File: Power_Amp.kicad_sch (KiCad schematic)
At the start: 22 parts, among them J10 2118718-2, J11 Molex 73251-1153, P13 CONUFL001-SMD-T, U27 TQP7M9106

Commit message: More notes and minor changes
Signed-off-by: Corey Minyard <corey@minyard.net>
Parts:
- removed R80: 0, Resistor_SMD:R_0603_1608Metric_Pad0.98x0.95mm_HandSolder, symbol Device:R
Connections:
- net at FL2.8 (INPUT): now also C117.2, L38.1
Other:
- note added: "2W (33dBm) into 50 ohms is 10V RMS, ~14.3V peak to peak on the right side of the impedance converter. Pick appropriate devices."
- moved on the sheet: FL2, J11, L39

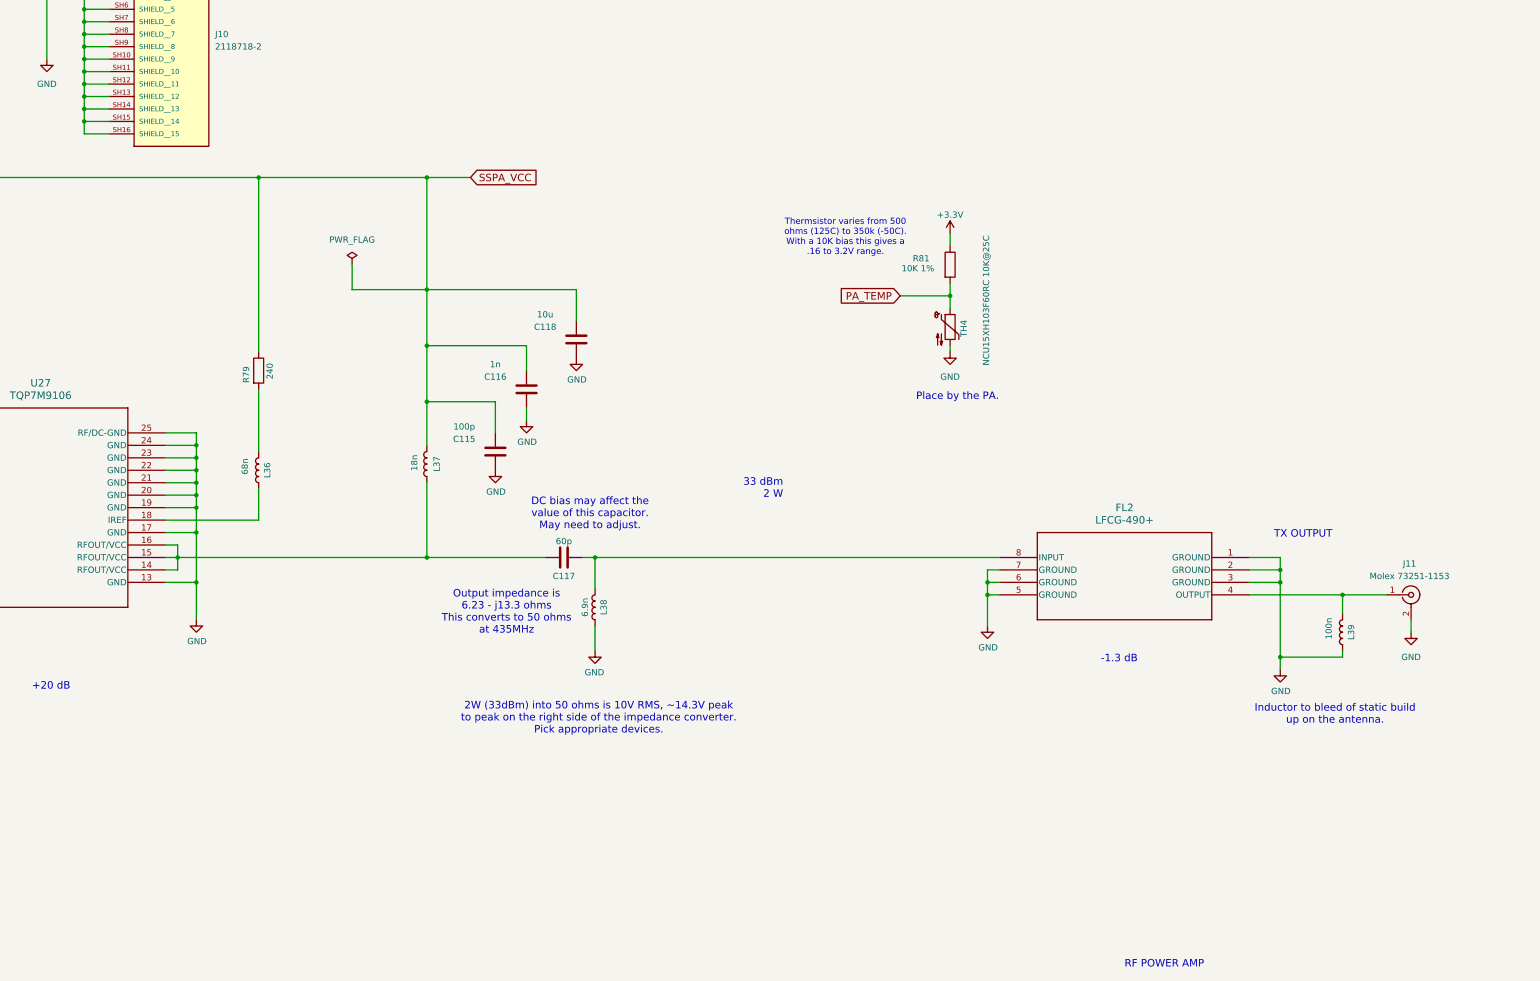
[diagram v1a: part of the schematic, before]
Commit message: Add power measurement on TX
Add chips for forward and reverse power.

Signed-off-by: Corey Minyard <corey@minyard.net>
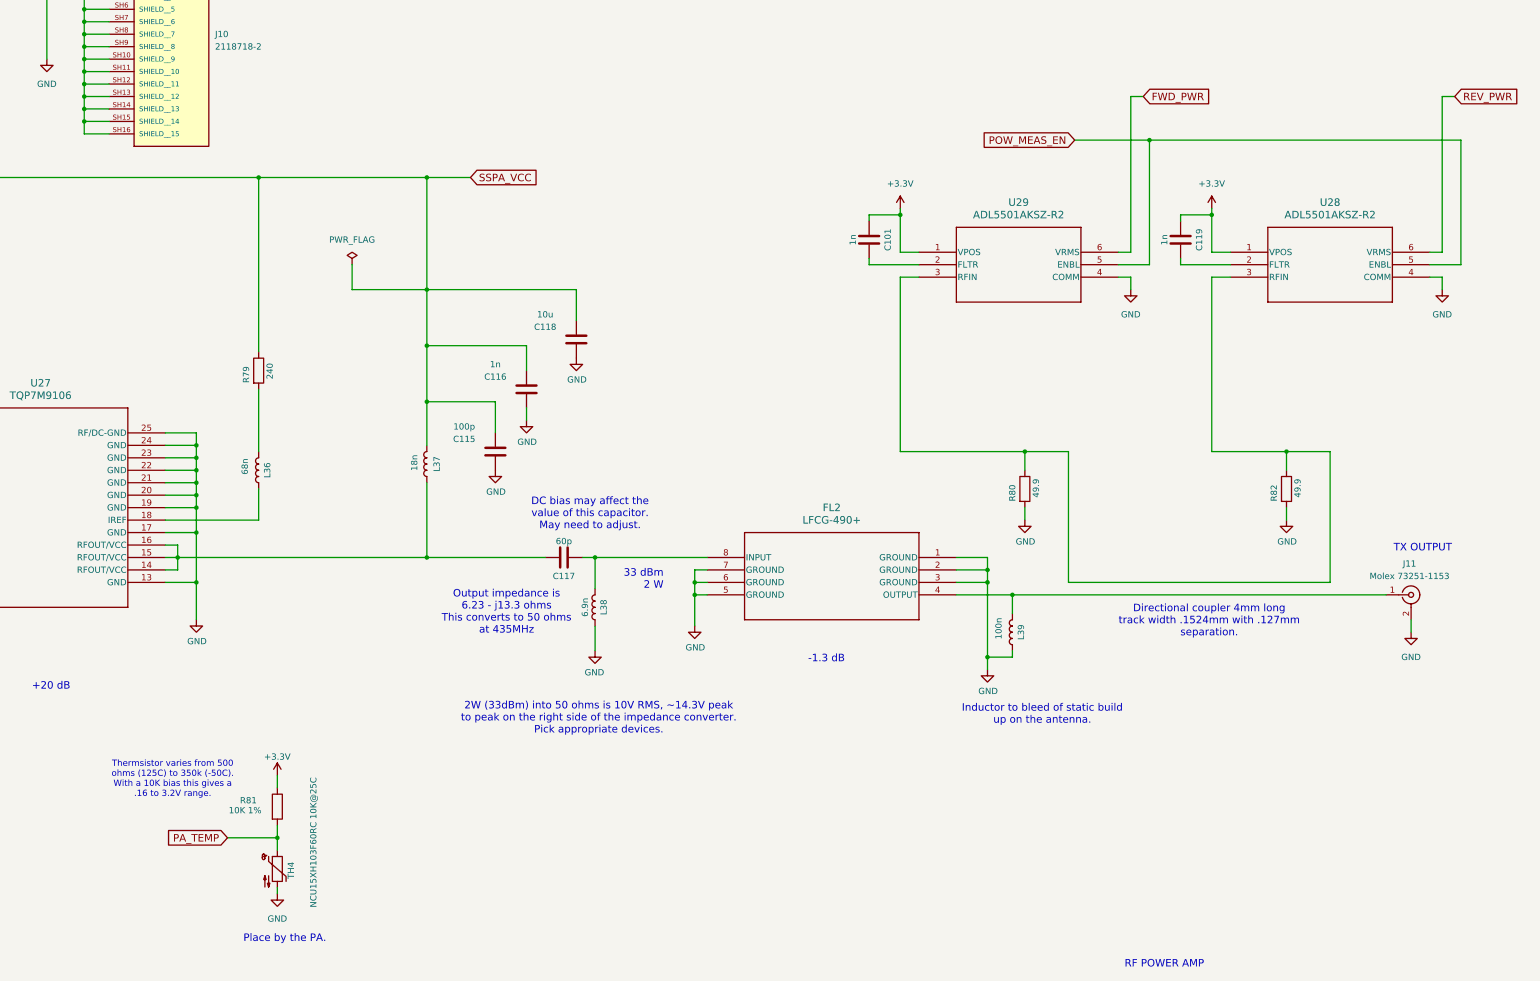
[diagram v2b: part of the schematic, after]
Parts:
- added C101, C119: 1n, Capacitor_SMD:C_0603_1608Metric_Pad1.08x0.95mm_HandSolder, symbol Device:C
- added R80, R82: 49.9, Resistor_SMD:R_0603_1608Metric_Pad0.98x0.95mm_HandSolder, symbol Device:R
- added U28, U29: ADL5501AKSZ-R2, PacSatDev_misc:KS-6_ADI, symbol PACSAT_ICs:ADL5501AKSZ-R2
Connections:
- net +3.3V: now also C101.2, C119.2, U28.1 (VPOS), U29.1 (VPOS)
- net GND: now also R80.2, R82.2, U28.4 (COMM), U29.4 (COMM)
- new net: C101.1, U29.2 (FLTR)
- new net: R80.1, R82.1, U28.3 (RFIN), U29.3 (RFIN)
- new net: C119.1, U28.2 (FLTR)
- new net FWD_PWR: U29.6 (VRMS)
- new net POW_MEAS_EN: U28.5 (ENBL), U29.5 (ENBL)
- new net REV_PWR: U28.6 (VRMS)
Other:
- note added: "Directional coupler 4mm long track width .1524mm with .127mm separation."
- moved on the sheet: FL2, L39, R81, TH4

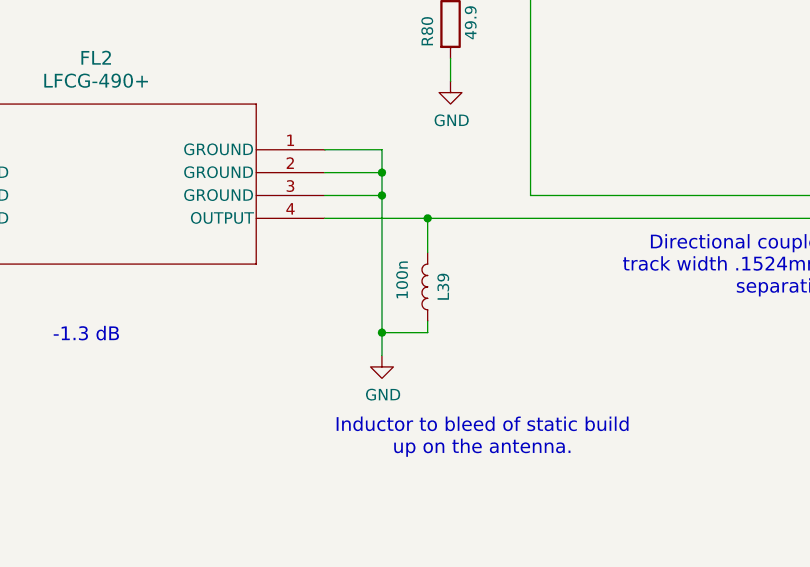
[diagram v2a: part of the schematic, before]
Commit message: Change TX bleed off inductor to bigger one
100nH really isn't big enough.

Signed-off-by: Corey Minyard <corey@minyard.net>
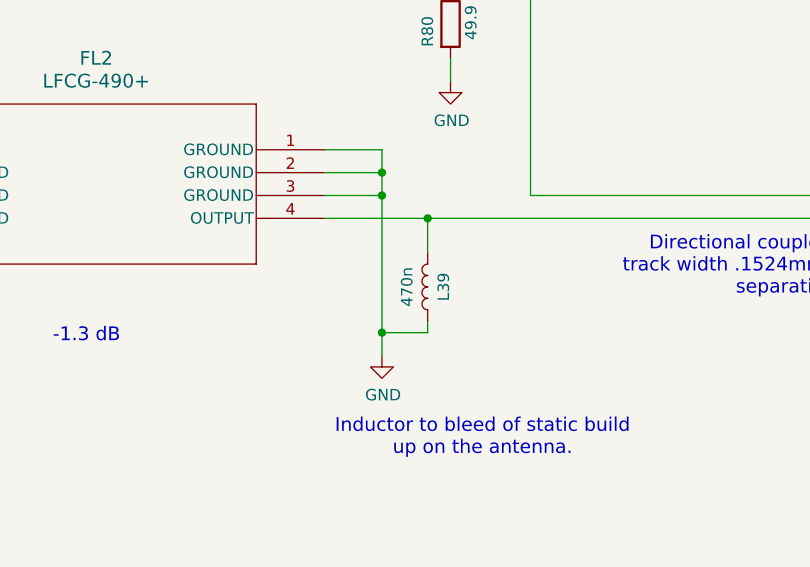
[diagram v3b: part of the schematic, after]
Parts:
- L39: value 100n -> 470n; footprint Inductor_SMD:L_0603_1608Metric_Pad1.05x0.95mm_HandSolder -> Inductor_SMD:L_0805_2012Metric_Pad1.15x1.40mm_HandSolder
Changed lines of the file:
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@@
 			)
 		)
-		(property "Value" "100n"
-			(at 310.896 174.498 90)
+		(property "Value" "470n"
+			(at 311.404 175.26 90)
 			(effects
 				(font
@@
 			)
 		)
-		(property "Footprint" "Inductor_SMD:L_0603_1608Metric_Pad1.05x0.95mm_HandSolder"
+		(property "Footprint" "Inductor_SMD:L_0805_2012Metric_Pad1.15x1.40mm_HandSolder"
 			(at 313.69 175.26 0)
 			(effects

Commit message: Check over notes and some component values
Fix a wrong capacitor in one spot, set Q and voltage as necessary.

Signed-off-by: Corey Minyard <corey@minyard.net>
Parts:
- added C57: 4p 1% 30V, Capacitor_SMD:C_0603_1608Metric_Pad1.08x0.95mm_HandSolder, symbol Device:C
- C114: value 37p -> 37p 1%
- C117: value 60p -> 110p 1% 30V
- L35: value 17n -> 17n 2% Q>=40
- L38: value 6.9n -> 6.8n 2% Q=40
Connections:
- net at C117.2, FL2.8 (INPUT), L38.1: now also C57.2
- net at C117.1, L37.1, U27.14 (RFOUT/VCC)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: now also C57.1
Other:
- note removed: "Class AB Use Hi Q Caps in all matching circuits (Ultra low ESR at 435 MHz)"
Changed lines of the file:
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@@
 	(text "DC bias may affect the\nvalue of this capacitor.\nMay need to adjust."
 		(exclude_from_sim no)
-		(at 227.584 151.13 0)
+		(at 243.078 155.194 0)
 		(effects
 			(font
@@
 		)
 	)
-	(text "\nClass AB \n\n\nUse Hi Q Caps in all matching circuits (Ultra low ESR at 435 MHz)"
-		(exclude_from_sim no)
-		(at 32.385 238.125 0)
-		(effects
-			(font
-				(size 1.524 1.524)
-			)
-			(justify left bottom)
-		)
-	)
 	(text "Output impedance is\n6.23 - j13.3 ohms\nThis converts to 50 ohms\nat 435MHz"
 		(exclude_from_sim no)
@@
 		(color 0 0 0 0)
 	)
+	(junction
+		(at 214.63 160.02)
+		(diameter 0)
+		(color 0 0 0 0)
+	)
 	(wire
 		(pts
@@
 	(wire
 		(pts
+			(xy 228.6 149.86) (xy 228.6 160.02)
+		)
+		(stroke
+			(width 0)
+			(type default)
+		)
+	)
+	(wire
+		(pts
 			(xy 143.51 160.02) (xy 194.31 160.02)
 		)
@@
 	(wire
 		(pts
+			(xy 214.63 149.86) (xy 214.63 160.02)
+		)
+		(stroke
+			(width 0)
+			(type default)
+		)
+	)
+	(wire
+		(pts
 			(xy 313.69 167.64) (xy 302.26 167.64)
 		)
@@
 	(wire
 		(pts
-			(xy 218.44 160.02) (xy 194.31 160.02)
+			(xy 218.44 160.02) (xy 214.63 160.02)
 		)
 		(stroke
@@
 	(wire
 		(pts
+			(xy 218.44 149.86) (xy 214.63 149.86)
+		)
+		(stroke
+			(width 0)
+			(type default)
+		)
+	)
+	(wire
+		(pts
 			(xy 194.31 82.55) (xy 194.31 105.41)
 		)
@@
 	(wire
 		(pts
+			(xy 214.63 160.02) (xy 194.31 160.02)
+		)
+		(stroke
+			(width 0)
+			(type default)
+		)
+	)
+	(wire
+		(pts
 			(xy 124.46 45.72) (xy 124.46 43.18)
 		)
@@
 	(wire
 		(pts
+			(xy 226.06 149.86) (xy 228.6 149.86)
+		)
+		(stroke
+			(width 0)
+			(type default)
+		)
+	)
+	(wire
+		(pts
 			(xy 398.78 102.87) (xy 401.32 102.87)
 		)
@@
 			)
 		)
-		(property "Value" "37p"
+		(property "Value" "37p 1%"
 			(at 78.74 154.94 0)
 			(effects
@@
 	)
 	(symbol
+		(lib_id "Device:C")
+		(at 222.25 149.86 90)
+		(mirror x)
+		(unit 1)
+		(exclude_from_sim no)
+		(in_bom yes)
+		(on_board yes)
+		(dnp no)
+		(property "Reference" "C57"
+			(at 222.25 153.67 90)
+			(effects
+				(font
+					(size 1.27 1.27)
+				)
+			)
+		)
+		(property "Value" "4p 1% 30V"
+			(at 222.25 146.558 90)
+			(effects
+				(font
+					(size 1.27 1.27)
+				)
+			)
+		)
+		(property "Footprint" "Capacitor_SMD:C_0603_1608Metric_Pad1.08x0.95mm_HandSolder"
+			(at 226.06 150.8252 0)
+			(effects
+				(font
+					(size 1.27 1.27)
+				)
+				(hide yes)
+			)
+		)
+		(property "Datasheet" "~"
+			(at 222.25 149.86 0)
+			(effects
+				(font
+					(size 1.27 1.27)
+				)
+				(hide yes)
+			)
+		)
+		(property "Description" ""
+			(at 222.25 149.86 0)
+			(effects
+				(font
+					(size 1.27 1.27)
+				)
+			)
+		)
+		(pin "1"
+		)
+		(pin "2"
+		)
+		(instances
+			(project "PacSat_AFSK"
+				(path "/cc9f42d2-6985-41ac-acab-5ab7b01c5b38/b85b88c3-87c5-49e2-804e-0759552ace3d"
+					(reference "C57")
+					(unit 1)
+				)
+			)
+		)
+	)
+	(symbol
 		(lib_id "power:GND")
 		(at 116.84 58.42 0)
@@
 			)
 		)
-		(property "Value" "60p"
+		(property "Value" "110p 1% 30V"
 			(at 222.25 156.718 90)
 			(effects
@@
 			)
 		)
-		(property "Value" "6.9n"
+		(property "Value" "6.8n 2% Q=40"
 			(at 226.568 170.18 90)
 			(effects
@@
 			)
 		)
-		(property "Value" "17n"
-			(at 79.502 139.446 90)
+		(property "Value" "17n 2% Q>=40"
+			(at 75.184 140.208 90)
 			(effects
 				(font

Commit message: Adjust the TX output impedance match some more
Signed-off-by: Corey Minyard <corey@minyard.net>
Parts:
- removed C57: 4p 1% 30V, Capacitor_SMD:C_0603_1608Metric_Pad1.08x0.95mm_HandSolder, symbol Device:C
- C117: value 110p 1% 30V -> 130p 1% 30V
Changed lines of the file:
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@@
 		(color 0 0 0 0)
 	)
-	(junction
-		(at 214.63 160.02)
-		(diameter 0)
-		(color 0 0 0 0)
-	)
 	(wire
 		(pts
@@
 	(wire
 		(pts
-			(xy 228.6 149.86) (xy 228.6 160.02)
-		)
-		(stroke
-			(width 0)
-			(type default)
-		)
-	)
-	(wire
-		(pts
 			(xy 143.51 160.02) (xy 194.31 160.02)
 		)
@@
 	(wire
 		(pts
-			(xy 214.63 149.86) (xy 214.63 160.02)
-		)
-		(stroke
-			(width 0)
-			(type default)
-		)
-	)
-	(wire
-		(pts
 			(xy 313.69 167.64) (xy 302.26 167.64)
 		)
@@
 	(wire
 		(pts
-			(xy 218.44 160.02) (xy 214.63 160.02)
+			(xy 194.31 160.02) (xy 218.44 160.02)
 		)
 		(stroke
@@
 	(wire
 		(pts
-			(xy 218.44 149.86) (xy 214.63 149.86)
-		)
-		(stroke
-			(width 0)
-			(type default)
-		)
-	)
-	(wire
-		(pts
 			(xy 194.31 82.55) (xy 194.31 105.41)
 		)
@@
 	(wire
 		(pts
-			(xy 214.63 160.02) (xy 194.31 160.02)
-		)
-		(stroke
-			(width 0)
-			(type default)
-		)
-	)
-	(wire
-		(pts
 			(xy 124.46 45.72) (xy 124.46 43.18)
 		)
@@
 	(wire
 		(pts
-			(xy 226.06 149.86) (xy 228.6 149.86)
-		)
-		(stroke
-			(width 0)
-			(type default)
-		)
-	)
-	(wire
-		(pts
 			(xy 398.78 102.87) (xy 401.32 102.87)
 		)
@@
 	)
 	(symbol
-		(lib_id "Device:C")
-		(at 222.25 149.86 90)
-		(mirror x)
-		(unit 1)
-		(exclude_from_sim no)
-		(in_bom yes)
-		(on_board yes)
-		(dnp no)
-		(property "Reference" "C57"
-			(at 222.25 153.67 90)
-			(effects
-				(font
-					(size 1.27 1.27)
-				)
-			)
-		)
-		(property "Value" "4p 1% 30V"
-			(at 222.25 146.558 90)
-			(effects
-				(font
-					(size 1.27 1.27)
-				)
-			)
-		)
-		(property "Footprint" "Capacitor_SMD:C_0603_1608Metric_Pad1.08x0.95mm_HandSolder"
-			(at 226.06 150.8252 0)
-			(effects
-				(font
-					(size 1.27 1.27)
-				)
-				(hide yes)
-			)
-		)
-		(property "Datasheet" "~"
-			(at 222.25 149.86 0)
-			(effects
-				(font
-					(size 1.27 1.27)
-				)
-				(hide yes)
-			)
-		)
-		(property "Description" ""
-			(at 222.25 149.86 0)
-			(effects
-				(font
-					(size 1.27 1.27)
-				)
-			)
-		)
-		(pin "1"
-		)
-		(pin "2"
-		)
-		(instances
-			(project "PacSat_AFSK"
-				(path "/cc9f42d2-6985-41ac-acab-5ab7b01c5b38/b85b88c3-87c5-49e2-804e-0759552ace3d"
-					(reference "C57")
-					(unit 1)
-				)
-			)
-		)
-	)
-	(symbol
 		(lib_id "power:GND")
 		(at 116.84 58.42 0)
@@
 			)
 		)
-		(property "Value" "110p 1% 30V"
+		(property "Value" "130p 1% 30V"
 			(at 222.25 156.718 90)
 			(effects

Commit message: More work on the LNA/PA impedance matchers
Did some simulations, found some issues.

Signed-off-by: Corey Minyard <corey@minyard.net>
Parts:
- C114: value 37p 1% -> 39p 1%
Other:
- moved on the sheet: C114, L35
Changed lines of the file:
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@@
 	(text "Input impedance is\n1.87 - 37.7j this\nmatches to 50 ohms\nat 435MHz."
 		(exclude_from_sim no)
-		(at 57.404 154.94 0)
+		(at 66.04 172.72 0)
 		(effects
 			(font
@@
 	)
 	(junction
-		(at 72.39 142.24)
-		(diameter 0)
-		(color 0 0 0 0)
-	)
-	(junction
 		(at 194.31 116.84)
 		(diameter 0)
@@
 	)
 	(junction
+		(at 58.42 142.24)
+		(diameter 0)
+		(color 0 0 0 0)
+	)
+	(junction
 		(at 83.82 162.56)
 		(diameter 0)
@@
 	(wire
 		(pts
-			(xy 50.8 142.24) (xy 72.39 142.24)
+			(xy 50.8 142.24) (xy 58.42 142.24)
 		)
 		(stroke
@@
 	(wire
 		(pts
-			(xy 72.39 142.24) (xy 74.93 142.24)
-		)
-		(stroke
-			(width 0)
-			(type default)
-		)
-	)
-	(wire
-		(pts
 			(xy 82.55 115.57) (xy 68.58 115.57)
 		)
@@
 	(wire
 		(pts
+			(xy 58.42 142.24) (xy 58.42 148.59)
+		)
+		(stroke
+			(width 0)
+			(type default)
+		)
+	)
+	(wire
+		(pts
 			(xy 369.57 138.43) (xy 369.57 142.24)
 		)
@@
 	(wire
 		(pts
+			(xy 69.85 142.24) (xy 87.63 142.24)
+		)
+		(stroke
+			(width 0)
+			(type default)
+		)
+	)
+	(wire
+		(pts
 			(xy 87.63 144.78) (xy 87.63 142.24)
 		)
@@
 	(wire
 		(pts
+			(xy 58.42 156.21) (xy 58.42 161.29)
+		)
+		(stroke
+			(width 0)
+			(type default)
+		)
+	)
+	(wire
+		(pts
 			(xy 124.46 55.88) (xy 124.46 53.34)
 		)
@@
 	(wire
 		(pts
-			(xy 72.39 156.21) (xy 72.39 161.29)
-		)
-		(stroke
-			(width 0)
-			(type default)
-		)
-	)
-	(wire
-		(pts
 			(xy 82.55 82.55) (xy 160.02 82.55)
 		)
@@
 	(wire
 		(pts
-			(xy 82.55 142.24) (xy 87.63 142.24)
+			(xy 58.42 142.24) (xy 62.23 142.24)
 		)
 		(stroke
@@
 	(wire
 		(pts
-			(xy 72.39 142.24) (xy 72.39 148.59)
-		)
-		(stroke
-			(width 0)
-			(type default)
-		)
-	)
-	(wire
-		(pts
 			(xy 354.33 102.87) (xy 358.14 102.87)
 		)
@@
 	(symbol
 		(lib_id "Device:C")
-		(at 72.39 152.4 0)
+		(at 58.42 152.4 0)
 		(unit 1)
 		(exclude_from_sim no)
@@
 		(dnp no)
 		(property "Reference" "C114"
-			(at 77.47 152.4 0)
+			(at 63.5 152.4 0)
 			(effects
 				(font
@@
 			)
 		)
-		(property "Value" "37p 1%"
-			(at 78.74 154.94 0)
+		(property "Value" "39p 1%"
+			(at 64.77 154.94 0)
 			(effects
 				(font
@@
 		)
 		(property "Footprint" "Capacitor_SMD:C_0603_1608Metric_Pad1.08x0.95mm_HandSolder"
-			(at 73.3552 156.21 0)
+			(at 59.3852 156.21 0)
 			(effects
 				(font
@@
 		)
 		(property "Datasheet" "~"
-			(at 72.39 152.4 0)
+			(at 58.42 152.4 0)
 			(effects
 				(font
@@
 		)
 		(property "Description" ""
-			(at 72.39 152.4 0)
+			(at 58.42 152.4 0)
 			(effects
 				(font
@@
 		)
 		(instances
-			(project "PacSat_Dev_RevD_240614"
+			(project "PacSat_AFSK"
 				(path "/cc9f42d2-6985-41ac-acab-5ab7b01c5b38/b85b88c3-87c5-49e2-804e-0759552ace3d"
 					(reference "C114")
@@
 	(symbol
 		(lib_id "power:GND")
-		(at 72.39 161.29 0)
+		(at 58.42 161.29 0)
 		(unit 1)
 		(exclude_from_sim no)
@@
 		(dnp no)
 		(property "Reference" "#PWR0222"
-			(at 72.39 167.64 0)
+			(at 58.42 167.64 0)
 			(effects
 				(font
@@
 		)
 		(property "Value" "GND"
-			(at 72.517 165.6842 0)
+			(at 58.547 165.6842 0)
 			(effects
 				(font
@@
 		)
 		(property "Footprint" ""
-			(at 72.39 161.29 0)
+			(at 58.42 161.29 0)
 			(effects
 				(font
@@
 		)
 		(property "Datasheet" ""
-			(at 72.39 161.29 0)
+			(at 58.42 161.29 0)
 			(effects
 				(font
@@
 		)
 		(property "Description" ""
-			(at 72.39 161.29 0)
+			(at 58.42 161.29 0)
 			(effects
 				(font
@@
 		)
 		(instances
-			(project "PacSat_Dev_RevD_240614"
+			(project "PacSat_AFSK"
 				(path "/cc9f42d2-6985-41ac-acab-5ab7b01c5b38/b85b88c3-87c5-49e2-804e-0759552ace3d"
 					(reference "#PWR0222")
@@
 	(symbol
 		(lib_id "Device:L")
-		(at 78.74 142.24 90)
+		(at 66.04 142.24 90)
 		(unit 1)
 		(exclude_from_sim no)
@@
 		(dnp no)
 		(property "Reference" "L35"
-			(at 78.74 144.018 90)
+			(at 66.04 144.018 90)
 			(effects
 				(font
@@
 		)
 		(property "Value" "17n 2% Q>=40"
-			(at 75.184 140.208 90)
+			(at 62.484 140.208 90)
 			(effects
 				(font
@@
 		)
 		(property "Footprint" "Inductor_SMD:L_0603_1608Metric_Pad1.05x0.95mm_HandSolder"
-			(at 78.74 142.24 0)
+			(at 66.04 142.24 0)
 			(effects
 				(font
@@
 		)
 		(property "Datasheet" "~"
-			(at 78.74 142.24 0)
+			(at 66.04 142.24 0)
 			(effects
 				(font
@@
 		)
 		(property "Description" ""
-			(at 78.74 142.24 0)
+			(at 66.04 142.24 0)
 			(effects
 				(font
@@
 		)
 		(instances
-			(project "PacSat_Dev_RevD_240614"
+			(project "PacSat_AFSK"
 				(path "/cc9f42d2-6985-41ac-acab-5ab7b01c5b38/b85b88c3-87c5-49e2-804e-0759552ace3d"
 					(reference "L35")
